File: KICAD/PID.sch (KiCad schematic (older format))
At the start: 23 parts, among them U1 AD8030

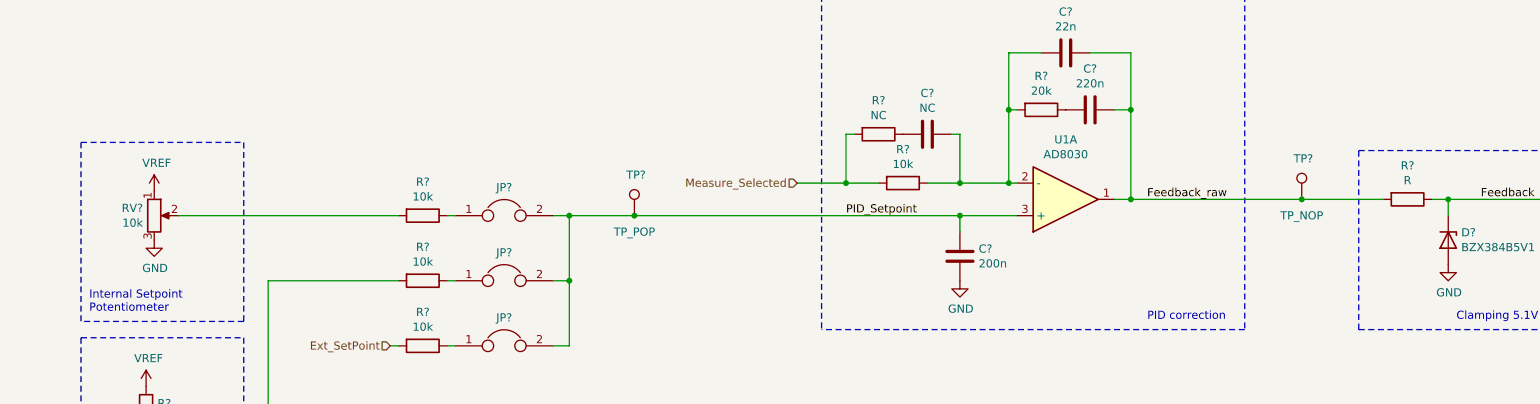
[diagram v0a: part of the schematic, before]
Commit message: drivers draft + clean and minors changes
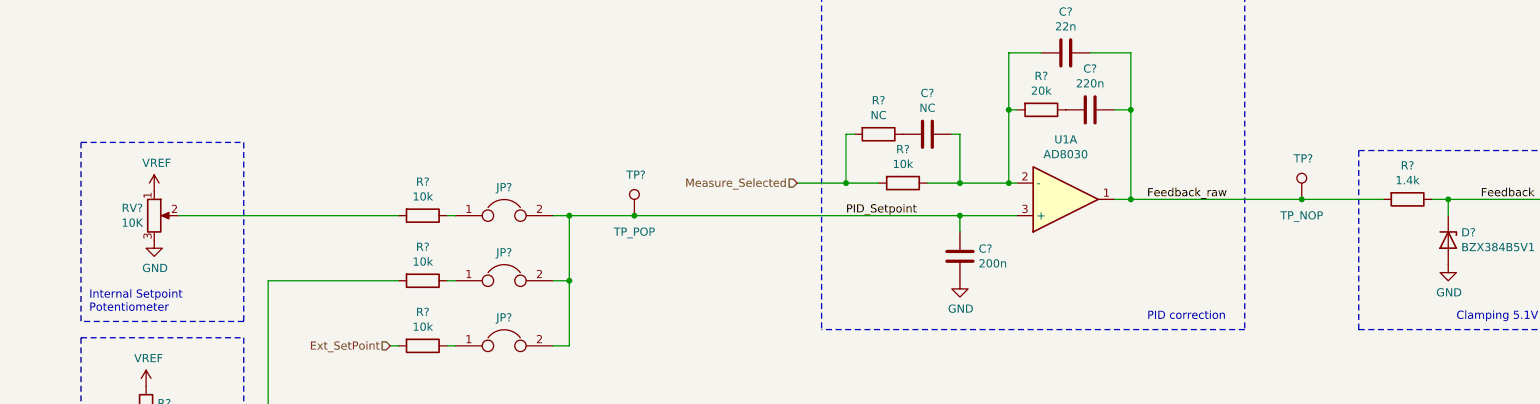
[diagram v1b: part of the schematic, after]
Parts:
- removed RV?: 10k, symbol Device:R_POT
- added RV?: 10K, Potentiometer_SMD:Potentiometer_Bourns_3214W_Vertical, symbol Device:R_POT
- R?: value R -> 1.4k
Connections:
- net GND: now also RV?.3
- net VREF: now also RV?.1
- net at R?.2: now also RV?.2
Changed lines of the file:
@@
 $Descr A4 11693 8268
 encoding utf-8
-Sheet 3 16
+Sheet 2 16
 Title "SESAME"
 Date ""
@@
 P 9350 3200
 F 0 "R?" V 9143 3200 50  0000 C CNN
-F 1 "R" V 9234 3200 50  0000 C CNN
+F 1 "1.4k" V 9234 3200 50  0000 C CNN
 F 2 "Resistor_SMD:R_0805_2012Metric_Pad1.15x1.40mm_HandSolder" V 9280 3200 50  0001 C CNN
 F 3 "~" H 9350 3200 50  0001 C CNN
@@
 	1    0    0    1
 $EndComp
-$Comp
-L Device:R_POT RV?
-U 1 1 615595FE
-P 1650 3300
-AR Path="/60F2F8DD/615595FE" Ref="RV?"  Part="1"
-AR Path="/60F1B237/615595FE" Ref="RV?"  Part="1"
-F 0 "RV?" H 1581 3346 50  0000 R CNN
-F 1 "10k" H 1581 3255 50  0000 R CNN
-F 2 "" H 1650 3300 50  0001 C CNN
-F 3 "~" H 1650 3300 50  0001 C CNN
-	1    1650 3300
-	1    0    0    -1
-$EndComp
 Wire Wire Line
 	1800 3300 3150 3300
@@
 Text Label 9800 3200 0    50   ~ 0
 Feedback
+$Comp
+L Device:R_POT RV?
+U 1 1 615B0664
+P 1650 3300
+AR Path="/60F2F8DD/615B0664" Ref="RV?"  Part="1"
+AR Path="/60F1B237/615B0664" Ref="RV?"  Part="1"
+F 0 "RV?" H 1581 3346 50  0000 R CNN
+F 1 "10K" H 1581 3255 50  0000 R CNN
+F 2 "Potentiometer_SMD:Potentiometer_Bourns_3214W_Vertical" H 1650 3300 50  0001 C CNN
+F 3 "https://docs.rs-online.com/0467/0900766b80025f51.pdf" H 1650 3300 50  0001 C CNN
+F 4 "3214W" H 1650 3300 50  0001 C CNN "Manifacturer_Ref"
+	1    1650 3300
+	1    0    0    -1
+$EndComp
 $EndSCHEMATC

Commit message: review w/ jmt
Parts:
- C1, C2, C3, C4, C5: renamed from C?; footprint Capacitor_SMD:C_0805_2012Metric_Pad1.15x1.40mm_HandSolder -> (none)
- R1, R2, R3, R4, R5, R6, R7, R8: renamed from R?; footprint Resistor_SMD:R_0805_2012Metric_Pad1.15x1.40mm_HandSolder -> (none)
- R9: renamed from R?; value 1.4k -> 390; footprint Resistor_SMD:R_0805_2012Metric_Pad1.15x1.40mm_HandSolder -> (none)
- U1: footprint Package_SO:SO-8_3.9x4.9mm_P1.27mm -> (none)
- gave numbers to parts that had none: 8

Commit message: edit footprints by jmt
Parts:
- C1, C2, C3, C4, C5: footprint (none) -> Capacitor_SMD:C_0805_2012Metric_Pad1.15x1.40mm_HandSolder
- JP1, JP2, JP3: footprint (none) -> Connector_PinHeader_2.54mm:PinHeader_1x02_P2.54mm_Vertical
- R1, R2, R3, R4, R5, R6, R7, R8, R9: footprint (none) -> Resistor_SMD:R_0805_2012Metric_Pad1.15x1.40mm_HandSolder
- TP2, TP4: footprint (none) -> TestPoint:TestPoint_Loop_D1.80mm_Drill1.0mm_Beaded
- TP3: footprint (none) -> TestPoint:TestPoint_THTPad_D2.0mm_Drill1.0mm
- U1: footprint (none) -> Package_SO:SO-8_5.3x6.2mm_P1.27mm
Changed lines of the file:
@@
 F 0 "C4" V 6998 2300 50  0000 C CNN
 F 1 "22n" V 7089 2300 50  0000 C CNN
-F 2 "" H 7288 2150 50  0001 C CNN
+F 2 "Capacitor_SMD:C_0805_2012Metric_Pad1.15x1.40mm_HandSolder" H 7288 2150 50  0001 C CNN
 F 3 "~" H 7250 2300 50  0001 C CNN
 	1    7250 2300
@@
 F 0 "R9" V 9143 3200 50  0000 C CNN
 F 1 "390" V 9234 3200 50  0000 C CNN
-F 2 "" V 9280 3200 50  0001 C CNN
+F 2 "Resistor_SMD:R_0805_2012Metric_Pad1.15x1.40mm_HandSolder" V 9280 3200 50  0001 C CNN
 F 3 "~" H 9350 3200 50  0001 C CNN
 	1    9350 3200
@@
 F 0 "C5" V 7148 2650 50  0000 C CNN
 F 1 "220n" V 7239 2650 50  0000 C CNN
-F 2 "" H 7438 2500 50  0001 C CNN
+F 2 "Capacitor_SMD:C_0805_2012Metric_Pad1.15x1.40mm_HandSolder" H 7438 2500 50  0001 C CNN
 F 3 "~" H 7400 2650 50  0001 C CNN
 	1    7400 2650
@@
 F 0 "R8" V 6893 2650 50  0000 C CNN
 F 1 "20k" V 6984 2650 50  0000 C CNN
-F 2 "" V 7030 2650 50  0001 C CNN
+F 2 "Resistor_SMD:R_0805_2012Metric_Pad1.15x1.40mm_HandSolder" V 7030 2650 50  0001 C CNN
 F 3 "~" H 7100 2650 50  0001 C CNN
 	1    7100 2650
@@
 F 0 "C2" V 6148 2800 50  0000 C CNN
 F 1 "NC" V 6239 2800 50  0000 C CNN
-F 2 "" H 6438 2650 50  0001 C CNN
+F 2 "Capacitor_SMD:C_0805_2012Metric_Pad1.15x1.40mm_HandSolder" H 6438 2650 50  0001 C CNN
 F 3 "~" H 6400 2800 50  0001 C CNN
 	1    6400 2800
@@
 F 0 "R6" V 5893 2800 50  0000 C CNN
 F 1 "NC" V 5984 2800 50  0000 C CNN
-F 2 "" V 6030 2800 50  0001 C CNN
+F 2 "Resistor_SMD:R_0805_2012Metric_Pad1.15x1.40mm_HandSolder" V 6030 2800 50  0001 C CNN
 F 3 "~" H 6100 2800 50  0001 C CNN
 	1    6100 2800
@@
 F 0 "C3" H 6715 3596 50  0000 L CNN
 F 1 "200n" H 6715 3505 50  0000 L CNN
-F 2 "" H 6638 3400 50  0001 C CNN
+F 2 "Capacitor_SMD:C_0805_2012Metric_Pad1.15x1.40mm_HandSolder" H 6638 3400 50  0001 C CNN
 F 3 "~" H 6600 3550 50  0001 C CNN
 	1    6600 3550
@@
 F 0 "R1" H 1670 4546 50  0000 L CNN
 F 1 "10k" H 1670 4455 50  0000 L CNN
-F 2 "" V 1530 4500 50  0001 C CNN
+F 2 "Resistor_SMD:R_0805_2012Metric_Pad1.15x1.40mm_HandSolder" V 1530 4500 50  0001 C CNN
 F 3 "~" H 1600 4500 50  0001 C CNN
 	1    1600 4500
@@
 F 0 "R2" H 1670 4946 50  0000 L CNN
 F 1 "10k" H 1670 4855 50  0000 L CNN
-F 2 "" V 1530 4900 50  0001 C CNN
+F 2 "Resistor_SMD:R_0805_2012Metric_Pad1.15x1.40mm_HandSolder" V 1530 4900 50  0001 C CNN
 F 3 "~" H 1600 4900 50  0001 C CNN
 	1    1600 4900
@@
 F 0 "JP3" H 3800 4273 50  0000 C CNN
 F 1 "Jumper" H 3800 4273 50  0001 C CNN
-F 2 "" H 3800 4100 50  0001 C CNN
+F 2 "Connector_PinHeader_2.54mm:PinHeader_1x02_P2.54mm_Vertical" H 3800 4100 50  0001 C CNN
 F 3 "~" H 3800 4100 50  0001 C CNN
 	1    3800 4100
@@
 F 0 "JP2" H 3800 3873 50  0000 C CNN
 F 1 "Jumper" H 3800 3873 50  0001 C CNN
-F 2 "" H 3800 3700 50  0001 C CNN
+F 2 "Connector_PinHeader_2.54mm:PinHeader_1x02_P2.54mm_Vertical" H 3800 3700 50  0001 C CNN
 F 3 "~" H 3800 3700 50  0001 C CNN
 	1    3800 3700
@@
 F 0 "R7" V 6043 3100 50  0000 C CNN
 F 1 "10k" V 6134 3100 50  0000 C CNN
-F 2 "" V 6180 3100 50  0001 C CNN
+F 2 "Resistor_SMD:R_0805_2012Metric_Pad1.15x1.40mm_HandSolder" V 6180 3100 50  0001 C CNN
 F 3 "~" H 6250 3100 50  0001 C CNN
 	1    6250 3100
@@
 F 0 "R4" V 3093 3700 50  0000 C CNN
 F 1 "10k" V 3184 3700 50  0000 C CNN
-F 2 "" V 3230 3700 50  0001 C CNN
+F 2 "Resistor_SMD:R_0805_2012Metric_Pad1.15x1.40mm_HandSolder" V 3230 3700 50  0001 C CNN
 F 3 "~" H 3300 3700 50  0001 C CNN
 	1    3300 3700
@@
 F 0 "R5" V 3093 4100 50  0000 C CNN
 F 1 "10k" V 3184 4100 50  0000 C CNN
-F 2 "" V 3230 4100 50  0001 C CNN
+F 2 "Resistor_SMD:R_0805_2012Metric_Pad1.15x1.40mm_HandSolder" V 3230 4100 50  0001 C CNN
 F 3 "~" H 3300 4100 50  0001 C CNN
 	1    3300 4100
@@
 F 0 "R3" V 3093 3300 50  0000 C CNN
 F 1 "10k" V 3184 3300 50  0000 C CNN
-F 2 "" V 3230 3300 50  0001 C CNN
+F 2 "Resistor_SMD:R_0805_2012Metric_Pad1.15x1.40mm_HandSolder" V 3230 3300 50  0001 C CNN
 F 3 "~" H 3300 3300 50  0001 C CNN
 	1    3300 3300
@@
 F 0 "C1" H 1565 6896 50  0000 L CNN
 F 1 "100n" H 1565 6805 50  0000 L CNN
-F 2 "" H 1488 6700 50  0001 C CNN
+F 2 "Capacitor_SMD:C_0805_2012Metric_Pad1.15x1.40mm_HandSolder" H 1488 6700 50  0001 C CNN
 F 3 "~" H 1450 6850 50  0001 C CNN
 	1    1450 6850
@@
 F 0 "U1" H 1063 6804 50  0000 R CNN
 F 1 "AD8030" H 1063 6895 50  0000 R CNN
-F 2 "" H 1250 6850 50  0001 C CNN
+F 2 "Package_SO:SO-8_5.3x6.2mm_P1.27mm" H 1250 6850 50  0001 C CNN
 F 3 "~" H 1250 6850 50  0001 C CNN
 	3    1250 6850
@@
 F 0 "U1" H 7250 2833 50  0000 C CNN
 F 1 "AD8030" H 7250 2924 50  0000 C CNN
-F 2 "" H 7250 3200 50  0001 C CNN
+F 2 "Package_SO:SO-8_5.3x6.2mm_P1.27mm" H 7250 3200 50  0001 C CNN
 F 3 "~" H 7250 3200 50  0001 C CNN
 	1    7250 3200
@@
 F 0 "JP1" H 3800 3473 50  0000 C CNN
 F 1 "Jumper" H 3800 3473 50  0001 C CNN
-F 2 "" H 3800 3300 50  0001 C CNN
+F 2 "Connector_PinHeader_2.54mm:PinHeader_1x02_P2.54mm_Vertical" H 3800 3300 50  0001 C CNN
 F 3 "~" H 3800 3300 50  0001 C CNN
 	1    3800 3300
@@
 F 0 "TP3" H 8650 3450 50  0000 L CNN
 F 1 "TP_NOP" H 8700 3100 50  0000 C CNN
-F 2 "" H 8900 3200 50  0001 C CNN
+F 2 "TestPoint:TestPoint_THTPad_D2.0mm_Drill1.0mm" H 8900 3200 50  0001 C CNN
 F 3 "~" H 8900 3200 50  0001 C CNN
 	1    8700 3200
@@
 F 0 "TP4" H 10450 3450 50  0000 L CNN
 F 1 "TP_POP" H 10500 3100 50  0000 C CNN
-F 2 "" H 10700 3200 50  0001 C CNN
+F 2 "TestPoint:TestPoint_Loop_D1.80mm_Drill1.0mm_Beaded" H 10700 3200 50  0001 C CNN
 F 3 "~" H 10700 3200 50  0001 C CNN
 	1    10500 3200
@@
 F 0 "TP2" H 4550 3550 50  0000 L CNN
 F 1 "TP_POP" H 4600 3200 50  0000 C CNN
-F 2 "" H 4800 3300 50  0001 C CNN
+F 2 "TestPoint:TestPoint_Loop_D1.80mm_Drill1.0mm_Beaded" H 4800 3300 50  0001 C CNN
 F 3 "~" H 4800 3300 50  0001 C CNN
 	1    4600 3300

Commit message: route + work on djd
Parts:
- C3: value 200n -> 470n
- R3, R4, R5: value 10k -> 47k
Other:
- note added: "23ms"
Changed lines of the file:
@@
 P 6600 3550
 F 0 "C3" H 6715 3596 50  0000 L CNN
-F 1 "200n" H 6715 3505 50  0000 L CNN
+F 1 "470n" H 6715 3505 50  0000 L CNN
 F 2 "Capacitor_SMD:C_0805_2012Metric_Pad1.15x1.40mm_HandSolder" H 6638 3400 50  0001 C CNN
 F 3 "~" H 6600 3550 50  0001 C CNN
@@
 P 3300 3700
 F 0 "R4" V 3093 3700 50  0000 C CNN
-F 1 "10k" V 3184 3700 50  0000 C CNN
+F 1 "47k" V 3184 3700 50  0000 C CNN
 F 2 "Resistor_SMD:R_0805_2012Metric_Pad1.15x1.40mm_HandSolder" V 3230 3700 50  0001 C CNN
 F 3 "~" H 3300 3700 50  0001 C CNN
@@
 P 3300 4100
 F 0 "R5" V 3093 4100 50  0000 C CNN
-F 1 "10k" V 3184 4100 50  0000 C CNN
+F 1 "47k" V 3184 4100 50  0000 C CNN
 F 2 "Resistor_SMD:R_0805_2012Metric_Pad1.15x1.40mm_HandSolder" V 3230 4100 50  0001 C CNN
 F 3 "~" H 3300 4100 50  0001 C CNN
@@
 P 3300 3300
 F 0 "R3" V 3093 3300 50  0000 C CNN
-F 1 "10k" V 3184 3300 50  0000 C CNN
+F 1 "47k" V 3184 3300 50  0000 C CNN
 F 2 "Resistor_SMD:R_0805_2012Metric_Pad1.15x1.40mm_HandSolder" V 3230 3300 50  0001 C CNN
 F 3 "~" H 3300 3300 50  0001 C CNN
@@
 	1    0    0    -1
 $EndComp
+Text Notes 6000 3700 0    100  ~ 0
+23ms
 $EndSCHEMATC

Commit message: added footprint for sepic coil + no more errors in netlist
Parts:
- C1, C2, C3, C4, C5: footprint Capacitor_SMD:C_0805_2012Metric_Pad1.15x1.40mm_HandSolder -> Sesame_footprint:C_0805_2012Metric_Pad1.18x1.45mm_HandSolder
- R1, R2, R3, R4, R5, R6, R7, R8, R9: footprint Resistor_SMD:R_0805_2012Metric_Pad1.15x1.40mm_HandSolder -> Sesame_footprint:R_0805_2012Metric_Pad1.20x1.40mm_HandSolder
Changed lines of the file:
@@
 F 0 "C4" V 6998 2300 50  0000 C CNN
 F 1 "22n" V 7089 2300 50  0000 C CNN
-F 2 "Capacitor_SMD:C_0805_2012Metric_Pad1.15x1.40mm_HandSolder" H 7288 2150 50  0001 C CNN
+F 2 "Sesame_footprint:C_0805_2012Metric_Pad1.18x1.45mm_HandSolder" H 7288 2150 50  0001 C CNN
 F 3 "~" H 7250 2300 50  0001 C CNN
 	1    7250 2300
@@
 F 0 "R9" V 9143 3200 50  0000 C CNN
 F 1 "390" V 9234 3200 50  0000 C CNN
-F 2 "Resistor_SMD:R_0805_2012Metric_Pad1.15x1.40mm_HandSolder" V 9280 3200 50  0001 C CNN
+F 2 "Sesame_footprint:R_0805_2012Metric_Pad1.20x1.40mm_HandSolder" V 9280 3200 50  0001 C CNN
 F 3 "~" H 9350 3200 50  0001 C CNN
 	1    9350 3200
@@
 F 0 "C5" V 7148 2650 50  0000 C CNN
 F 1 "220n" V 7239 2650 50  0000 C CNN
-F 2 "Capacitor_SMD:C_0805_2012Metric_Pad1.15x1.40mm_HandSolder" H 7438 2500 50  0001 C CNN
+F 2 "Sesame_footprint:C_0805_2012Metric_Pad1.18x1.45mm_HandSolder" H 7438 2500 50  0001 C CNN
 F 3 "~" H 7400 2650 50  0001 C CNN
 	1    7400 2650
@@
 F 0 "R8" V 6893 2650 50  0000 C CNN
 F 1 "20k" V 6984 2650 50  0000 C CNN
-F 2 "Resistor_SMD:R_0805_2012Metric_Pad1.15x1.40mm_HandSolder" V 7030 2650 50  0001 C CNN
+F 2 "Sesame_footprint:R_0805_2012Metric_Pad1.20x1.40mm_HandSolder" V 7030 2650 50  0001 C CNN
 F 3 "~" H 7100 2650 50  0001 C CNN
 	1    7100 2650
@@
 F 0 "C2" V 6148 2800 50  0000 C CNN
 F 1 "NC" V 6239 2800 50  0000 C CNN
-F 2 "Capacitor_SMD:C_0805_2012Metric_Pad1.15x1.40mm_HandSolder" H 6438 2650 50  0001 C CNN
+F 2 "Sesame_footprint:C_0805_2012Metric_Pad1.18x1.45mm_HandSolder" H 6438 2650 50  0001 C CNN
 F 3 "~" H 6400 2800 50  0001 C CNN
 	1    6400 2800
@@
 F 0 "R6" V 5893 2800 50  0000 C CNN
 F 1 "NC" V 5984 2800 50  0000 C CNN
-F 2 "Resistor_SMD:R_0805_2012Metric_Pad1.15x1.40mm_HandSolder" V 6030 2800 50  0001 C CNN
+F 2 "Sesame_footprint:R_0805_2012Metric_Pad1.20x1.40mm_HandSolder" V 6030 2800 50  0001 C CNN
 F 3 "~" H 6100 2800 50  0001 C CNN
 	1    6100 2800
@@
 F 0 "C3" H 6715 3596 50  0000 L CNN
 F 1 "470n" H 6715 3505 50  0000 L CNN
-F 2 "Capacitor_SMD:C_0805_2012Metric_Pad1.15x1.40mm_HandSolder" H 6638 3400 50  0001 C CNN
+F 2 "Sesame_footprint:C_0805_2012Metric_Pad1.18x1.45mm_HandSolder" H 6638 3400 50  0001 C CNN
 F 3 "~" H 6600 3550 50  0001 C CNN
 	1    6600 3550
@@
 F 0 "R1" H 1670 4546 50  0000 L CNN
 F 1 "10k" H 1670 4455 50  0000 L CNN
-F 2 "Resistor_SMD:R_0805_2012Metric_Pad1.15x1.40mm_HandSolder" V 1530 4500 50  0001 C CNN
+F 2 "Sesame_footprint:R_0805_2012Metric_Pad1.20x1.40mm_HandSolder" V 1530 4500 50  0001 C CNN
 F 3 "~" H 1600 4500 50  0001 C CNN
 	1    1600 4500
@@
 F 0 "R2" H 1670 4946 50  0000 L CNN
 F 1 "10k" H 1670 4855 50  0000 L CNN
-F 2 "Resistor_SMD:R_0805_2012Metric_Pad1.15x1.40mm_HandSolder" V 1530 4900 50  0001 C CNN
+F 2 "Sesame_footprint:R_0805_2012Metric_Pad1.20x1.40mm_HandSolder" V 1530 4900 50  0001 C CNN
 F 3 "~" H 1600 4900 50  0001 C CNN
 	1    1600 4900
@@
 F 0 "R7" V 6043 3100 50  0000 C CNN
 F 1 "10k" V 6134 3100 50  0000 C CNN
-F 2 "Resistor_SMD:R_0805_2012Metric_Pad1.15x1.40mm_HandSolder" V 6180 3100 50  0001 C CNN
+F 2 "Sesame_footprint:R_0805_2012Metric_Pad1.20x1.40mm_HandSolder" V 6180 3100 50  0001 C CNN
 F 3 "~" H 6250 3100 50  0001 C CNN
 	1    6250 3100
@@
 F 0 "R4" V 3093 3700 50  0000 C CNN
 F 1 "47k" V 3184 3700 50  0000 C CNN
-F 2 "Resistor_SMD:R_0805_2012Metric_Pad1.15x1.40mm_HandSolder" V 3230 3700 50  0001 C CNN
+F 2 "Sesame_footprint:R_0805_2012Metric_Pad1.20x1.40mm_HandSolder" V 3230 3700 50  0001 C CNN
 F 3 "~" H 3300 3700 50  0001 C CNN
 	1    3300 3700
@@
 F 0 "R5" V 3093 4100 50  0000 C CNN
 F 1 "47k" V 3184 4100 50  0000 C CNN
-F 2 "Resistor_SMD:R_0805_2012Metric_Pad1.15x1.40mm_HandSolder" V 3230 4100 50  0001 C CNN
+F 2 "Sesame_footprint:R_0805_2012Metric_Pad1.20x1.40mm_HandSolder" V 3230 4100 50  0001 C CNN
 F 3 "~" H 3300 4100 50  0001 C CNN
 	1    3300 4100
@@
 F 0 "R3" V 3093 3300 50  0000 C CNN
 F 1 "47k" V 3184 3300 50  0000 C CNN
-F 2 "Resistor_SMD:R_0805_2012Metric_Pad1.15x1.40mm_HandSolder" V 3230 3300 50  0001 C CNN
+F 2 "Sesame_footprint:R_0805_2012Metric_Pad1.20x1.40mm_HandSolder" V 3230 3300 50  0001 C CNN
 F 3 "~" H 3300 3300 50  0001 C CNN
 	1    3300 3300
@@
 F 0 "C1" H 1565 6896 50  0000 L CNN
 F 1 "100n" H 1565 6805 50  0000 L CNN
-F 2 "Capacitor_SMD:C_0805_2012Metric_Pad1.15x1.40mm_HandSolder" H 1488 6700 50  0001 C CNN
+F 2 "Sesame_footprint:C_0805_2012Metric_Pad1.18x1.45mm_HandSolder" H 1488 6700 50  0001 C CNN
 F 3 "~" H 1450 6850 50  0001 C CNN
 	1    1450 6850

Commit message: lil cleanup on the main schematic sheet
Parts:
- C1, C2, C3, C4, C5: symbol Device:C -> sesame-fonctionnel-rescue:C-Device
- D1: symbol Device:D_Zener -> sesame-fonctionnel-rescue:D_Zener-Device
- JP1, JP2, JP3: symbol Device:Jumper -> sesame-fonctionnel-rescue:Jumper-Device
- R1, R2, R3, R4, R5, R6, R7, R8, R9: symbol Device:R -> sesame-fonctionnel-rescue:R-Device
- RV1: symbol Device:R_POT -> sesame-fonctionnel-rescue:R_POT-Device
- TP2, TP3, TP4: symbol Connector:TestPoint -> sesame-fonctionnel-rescue:TestPoint-Connector
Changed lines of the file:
@@
 	6900 2650 6900 3100
 $Comp
-L Device:C C4
+L sesame-fonctionnel-rescue:C-Device C4
 U 1 1 6143D584
 P 7250 2300
@@
 	7650 2650 7650 3200
 $Comp
-L Device:D_Zener D1
+L sesame-fonctionnel-rescue:D_Zener-Device D1
 U 1 1 61442454
 P 9600 3450
@@
 $EndComp
 $Comp
-L Device:R R9
+L sesame-fonctionnel-rescue:R-Device R9
 U 1 1 61442D7B
 P 9350 3200
@@
 Connection ~ 9600 3200
 $Comp
-L power:GND #PWR010
+L sesame-fonctionnel-rescue:GND-power #PWR010
 U 1 1 614457E8
 P 9600 3600
@@
 	9050 4000 10250 4000
 $Comp
-L Device:C C5
+L sesame-fonctionnel-rescue:C-Device C5
 U 1 1 6143E2B5
 P 7400 2650
@@
 $EndComp
 $Comp
-L Device:R R8
+L sesame-fonctionnel-rescue:R-Device R8
 U 1 1 614317CF
 P 7100 2650
@@
 $EndComp
 $Comp
-L Device:C C2
+L sesame-fonctionnel-rescue:C-Device C2
 U 1 1 611CBEF7
 P 6400 2800
@@
 $EndComp
 $Comp
-L Device:R R6
+L sesame-fonctionnel-rescue:R-Device R6
 U 1 1 611CBEFD
 P 6100 2800
@@
 Connection ~ 6900 3100
 $Comp
-L Device:C C3
+L sesame-fonctionnel-rescue:C-Device C3
 U 1 1 611D6D98
 P 6600 3550
@@
 $EndComp
 $Comp
-L power:GND #PWR09
+L sesame-fonctionnel-rescue:GND-power #PWR09
 U 1 1 611DA84B
 P 6600 3700
@@
 	5750 1950 8350 1950
 $Comp
-L power:GND #PWR?
+L sesame-fonctionnel-rescue:GND-power #PWR?
 U 1 1 615595F8
 P 1600 5050
@@
 $EndComp
 $Comp
-L power:GND #PWR?
+L sesame-fonctionnel-rescue:GND-power #PWR?
 U 1 1 61559604
 P 1650 3450
@@
 $EndComp
 $Comp
-L Device:R R?
+L sesame-fonctionnel-rescue:R-Device R?
 U 1 1 6155960A
 P 1600 4500
@@
 $EndComp
 $Comp
-L Device:R R?
+L sesame-fonctionnel-rescue:R-Device R?
 U 1 1 61559610
 P 1600 4900
@@
 	2200 4050 2200 5550
 $Comp
-L Device:Jumper JP3
+L sesame-fonctionnel-rescue:Jumper-Device JP3
 U 1 1 6141B2EB
 P 3800 4100
@@
 $EndComp
 $Comp
-L Device:Jumper JP2
+L sesame-fonctionnel-rescue:Jumper-Device JP2
 U 1 1 6141B2F1
 P 3800 3700
@@
 Ext_SetPoint
 $Comp
-L Device:R R7
+L sesame-fonctionnel-rescue:R-Device R7
 U 1 1 61401A0F
 P 6250 3100
@@
 	3450 3700 3500 3700
 $Comp
-L Device:R R4
+L sesame-fonctionnel-rescue:R-Device R4
 U 1 1 61416962
 P 3300 3700
@@
 $EndComp
 $Comp
-L Device:R R5
+L sesame-fonctionnel-rescue:R-Device R5
 U 1 1 611D5F7E
 P 3300 4100
@@
 $EndComp
 $Comp
-L Device:R R3
+L sesame-fonctionnel-rescue:R-Device R3
 U 1 1 612A4BF5
 P 3300 3300
@@
 Connection ~ 6600 3300
 $Comp
-L Device:C C?
+L sesame-fonctionnel-rescue:C-Device C?
 U 1 1 6124BDDF
 P 1450 6850
@@
 	1150 7200 1150 7150
 $Comp
-L power:GND #PWR?
+L sesame-fonctionnel-rescue:GND-power #PWR?
 U 1 1 6124BDEA
 P 1300 7250
@@
 	1300 7200 1450 7200
 $Comp
-L power:VCC #PWR?
+L sesame-fonctionnel-rescue:VCC-power #PWR?
 U 1 1 6124BDF7
 P 1300 6450
@@
 	1800 3300 3150 3300
 $Comp
-L Device:Jumper JP1
+L sesame-fonctionnel-rescue:Jumper-Device JP1
 U 1 1 612A8A2A
 P 3800 3300
@@
 	3500 3300 3450 3300
 $Comp
-L Connector:TestPoint TP?
+L sesame-fonctionnel-rescue:TestPoint-Connector TP?
 U 1 1 612E229E
 P 8700 3200
@@
 	8700 3200 7650 3200
 $Comp
-L Connector:TestPoint TP?
+L sesame-fonctionnel-rescue:TestPoint-Connector TP?
 U 1 1 612E6FF3
 P 10500 3200
@@
 	10500 3200 10700 3200
 $Comp
-L Connector:TestPoint TP?
+L sesame-fonctionnel-rescue:TestPoint-Connector TP?
 U 1 1 612EF9C2
 P 4600 3300
@@
 Feedback
 $Comp
-L Device:R_POT RV?
+L sesame-fonctionnel-rescue:R_POT-Device RV?
 U 1 1 615B0664
 P 1650 3300
